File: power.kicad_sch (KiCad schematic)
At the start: 30 parts, among them U201 XC6206PxxxMR, U202 XR76208

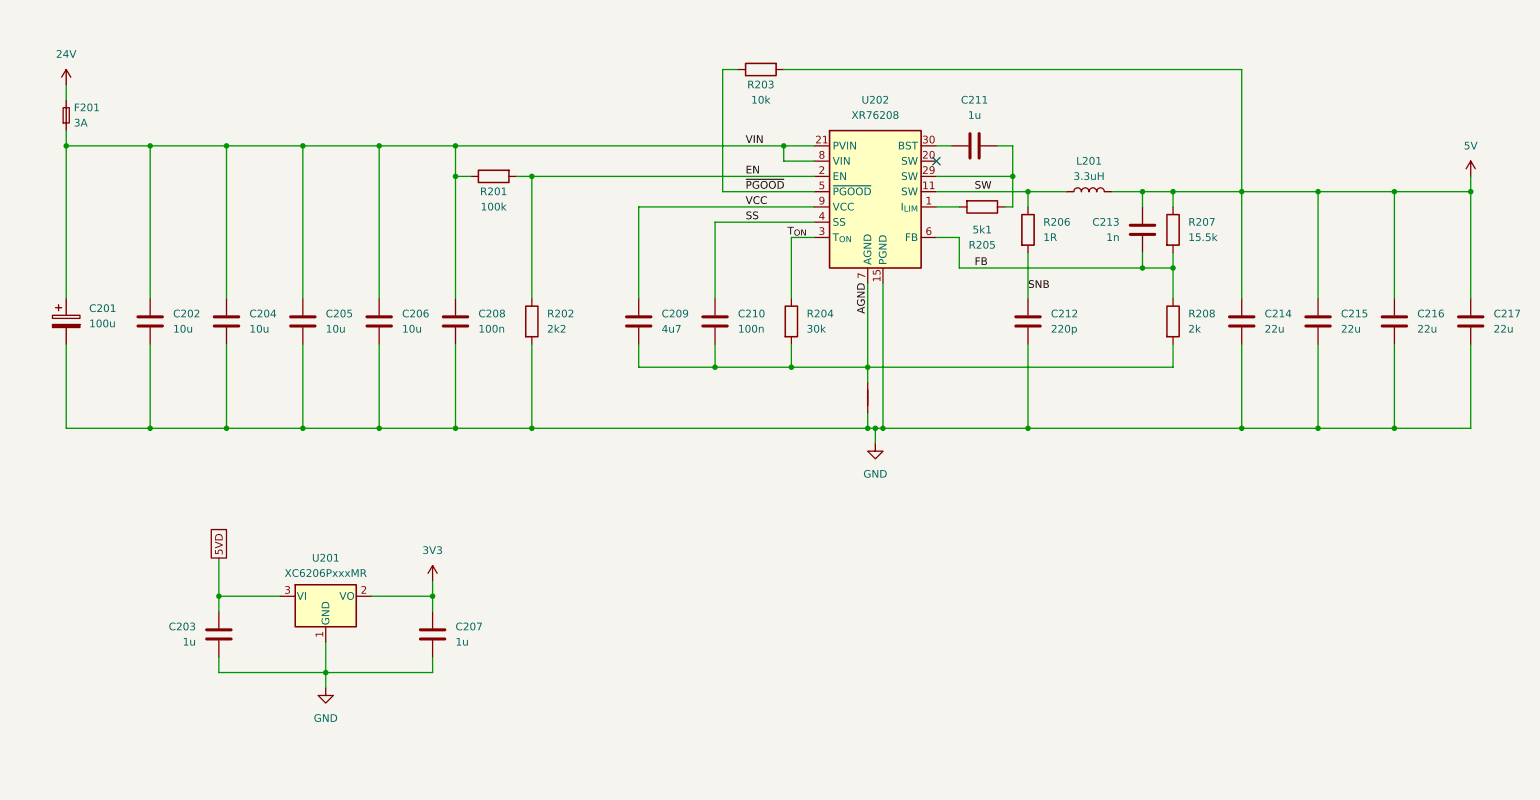
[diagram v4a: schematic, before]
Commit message: Rev 0.2: Major hardware improvements and production readiness
Hardware Improvements (Thanks to shx for schematic cleanup):
- Clean up schematic organization and structure
- Set CAN transceiver Silent pin to GND for stability
- Add status LEDs (yellow: 24V/5V/3.3V, green: MCU PB4)
- Replace jumpers with solder jumpers on bottom side
- Add jumpers to output PFETs for permanent-on without firmware
- Add robust test points for 5V/GND load testing
- Add optional heatsink for DC/DC converter on bottom
- Add 10µF capacitor for MCU on 3.3V rail

Component Optimizations:
- Replace 30kΩ with 33kΩ basic part for simplified BOM
- Change DC/DC feedback: 15.5kΩ15kΩ (new output: 5.1V)
- Upgrade CAN ESD protection: NUP2105LPESD1CAN
- Increase CAN termination resistor footprint: 04020603
- Switch USB hub supply from 5V to 3.3V per datasheet

Production Ready:
- Add all LCSC part numbers and rotations
- Generate complete production data package
- Improve PCB layout and button placement
- Create comprehensive changelog documentation
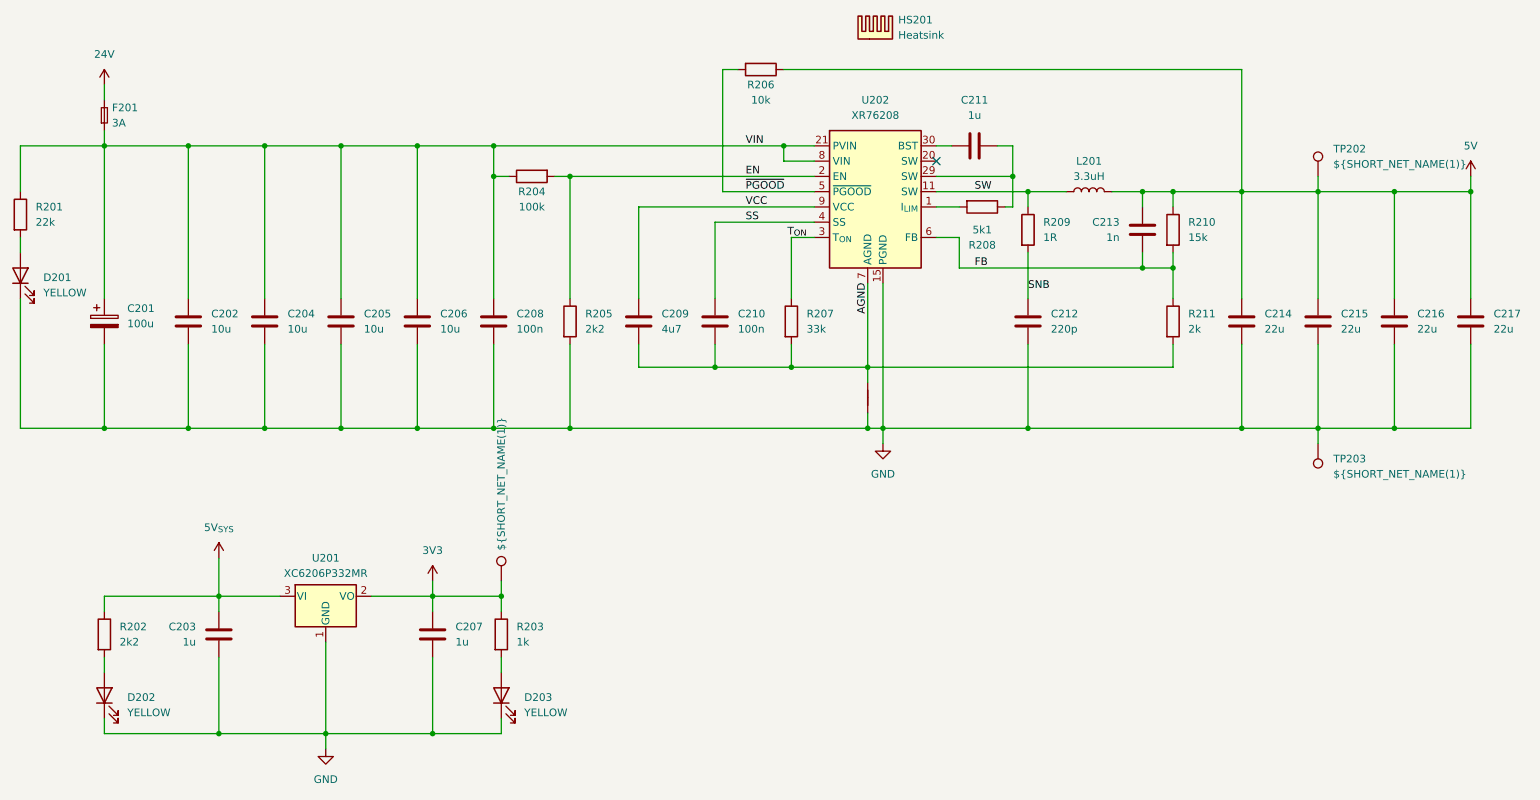
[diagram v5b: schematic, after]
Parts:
- added D201, D202, D203: YELLOW, LED_SMD:LED_0805_2012Metric, symbol Device:LED
- added HS201: Heatsink, project:HeatSink_9x9x5, symbol Mechanical:Heatsink
- added R201: 22k, Resistor_SMD:R_0402_1005Metric, symbol Device:R
- added R202: 2k2, Resistor_SMD:R_0402_1005Metric, symbol Device:R
- added R203: 1k, Resistor_SMD:R_0402_1005Metric, symbol Device:R
- added TP201: ${SHORT_NET_NAME(1)}, project:NAMED_TEST_POINT, symbol project:NamedTestPoint
- added TP202, TP203: ${SHORT_NET_NAME(1)}, TestPoint:TestPoint_Pad_D3.0mm, symbol Connector:TestPoint
- C203, C207, C211: LCSC Part # (none) -> C52923; Manufacturer Part # (none) -> CL05A105KA5NQNC
- C208, C210: LCSC Part # (none) -> C307331; Manufacturer Part # (none) -> CL05B104KB54PNC
- C212: LCSC Part # (none) -> C1603; Manufacturer Part # (none) -> CL10B221KB8NNNC
- C213: LCSC Part # (none) -> C1523; Manufacturer Part # (none) -> 0402B102K500NT
- C214, C215, C216, C217: LCSC Part # (none) -> C12891; Manufacturer Part # (none) -> CL31A226KAHNNNE
- F201: LCSC Part # (none) -> C163126; Manufacturer Part # (none) -> CFS12V3T3R00
- R204: renamed from R201; LCSC Part # (none) -> C25741; Manufacturer Part # (none) -> 0402WGF1003TCE
- R205: renamed from R202; LCSC Part # (none) -> C25879; Manufacturer Part # (none) -> 0402WGF2201TCE
- R206: renamed from R203; LCSC Part # (none) -> C25744; Manufacturer Part # (none) -> 0402WGF1002TCE
- R207: renamed from R204; value 30k -> 33k; LCSC Part # (none) -> C25779; Manufacturer Part # (none) -> 0402WGF3302TCE
- R208: renamed from R205; LCSC Part # (none) -> C25905; Manufacturer Part # (none) -> 0402WGF5101TCE
- R209: renamed from R206; LCSC Part # (none) -> C22936; Manufacturer Part # (none) -> 0603WAF100KT5E
- R210: renamed from R207; value 15.5k -> 15k; LCSC Part # (none) -> C25756; Manufacturer Part # (none) -> 0402WGF1502TCE
- R211: renamed from R208; LCSC Part # (none) -> C4109; Manufacturer Part # (none) -> 0402WGF2001TCE
- U201: value XC6206PxxxMR -> XC6206P332MR; LCSC Part # (none) -> C5446; Manufacturer Part # (none) -> XC6206P332MR-G
- U202: LCSC Part # (none) -> C555356; Manufacturer Part # (none) -> XR76208ELTR-F
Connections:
- net 3V3: now also R203.1, TP201.1
- net 5V: now also R206.1, TP202.1; no longer R206.2
- net AGND: no longer U202.31 (AGND)
- net GND: now also D201.1 (K), D202.1 (K), D203.1 (K), TP203.1
- net VIN: now also R201.1
- net ~{PGOOD}: now also R206.2; no longer R206.1
- net 5VD renamed 5V_{SYS}
- net 5V_{SYS}: now also R202.1
- new net: D202.2 (A), R202.2
- new net: D203.2 (A), R203.2
- new net: D201.2 (A), R201.2
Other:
- moved on the sheet: C201, C202, C204, C205, C206, C208, F201, R204, R205, R206

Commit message: Rev. 0.3: Add 10µF capacitor C304 to CAN transceiver and QR code placeholder
- Added 10µF capacitor C304 for improved CAN communication stability
- Added QR code placeholder for serial number on PCB
- Enhanced signal integrity with additional filtering at CAN transceiver
- Improved traceability with unique identification capability
- Updated changelogs and documentation for Rev. 0.3
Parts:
- U202: footprint project:IC_XR76203ELTR-F -> project:IC_XR76208ELTR-F
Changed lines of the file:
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@@
 			)
 		)
-		(property "Footprint" "project:IC_XR76203ELTR-F"
+		(property "Footprint" "project:IC_XR76208ELTR-F"
 			(at 163.83 63.5 0)
 			(effects

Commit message: Production Optimization: JLCPCB assembly improvements
- Excluded test points TP202/TP203 from BOM
- Set FT rotation offsets for automated assembly:
  - U202/U301: 270° rotation offset
  - U401: 180° rotation offset
- Updated production data for JLCPCB compatibility
- Added unreleased changelog section for tracking
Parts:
- TP202, TP203: now left out of the parts list
- U202: FT Rotation Offset (none) -> 270
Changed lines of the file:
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@@
 		(unit 1)
 		(exclude_from_sim no)
-		(in_bom yes)
+		(in_bom no)
 		(on_board yes)
 		(dnp no)
@@
 		(unit 1)
 		(exclude_from_sim no)
-		(in_bom yes)
+		(in_bom no)
 		(on_board yes)
 		(dnp no)
@@
 			(at 163.83 63.5 0)
 			(effects
+				(font
+					(size 1.27 1.27)
+				)
+				(hide yes)
+			)
+		)
+		(property "FT Rotation Offset" "270"
+			(at 163.83 63.5 0)
+			(effects

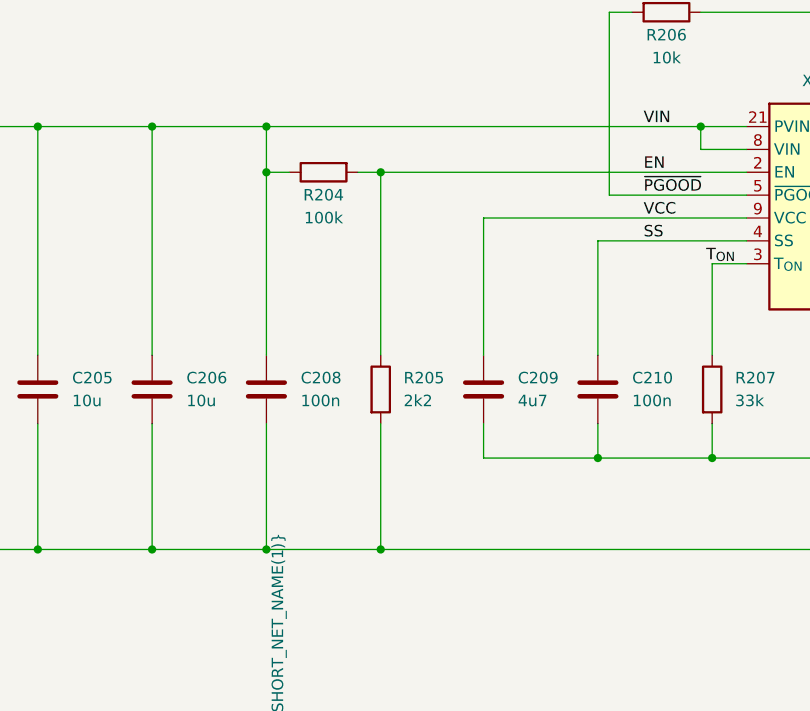
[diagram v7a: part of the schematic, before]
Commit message: docs: Update unreleased changes in changelog and README
- Fixed USB hub controller (U401/CH334): XO pin connected to GND for crystal-less operation
- Fixed DC/DC converter (U202/XR76208): Enable circuit changed to Zener diode for 12V operation
- Fixed USB outputs: Replaced fuses with TPS2557 power distribution switches for backfeed protection
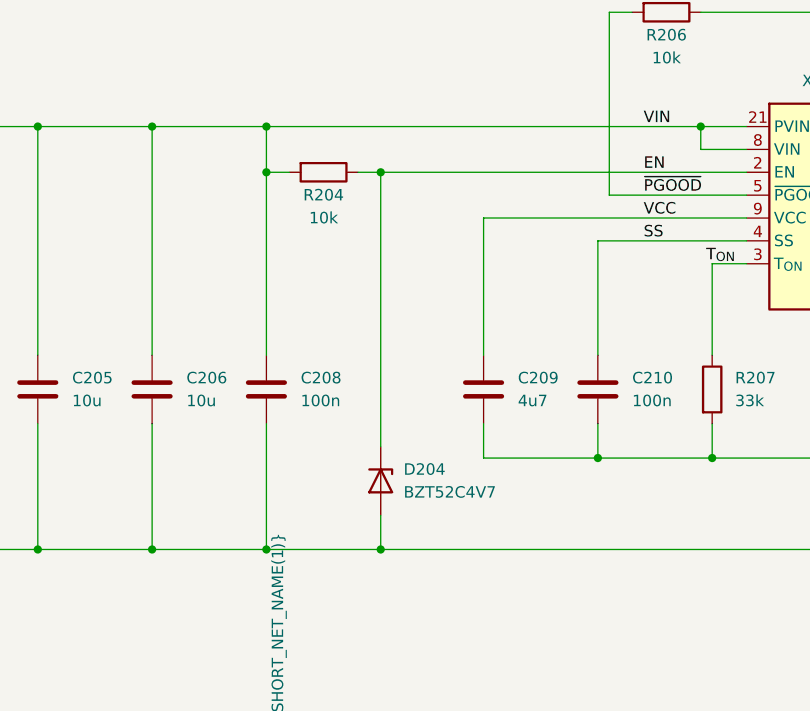
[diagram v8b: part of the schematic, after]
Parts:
- removed R205: 2k2, Resistor_SMD:R_0402_1005Metric, symbol Device:R
- added D204: BZT52C4V7, Diode_SMD:D_SOD-123, symbol Device:D_Zener
- R204: value 100k -> 10k; LCSC Part # C25741 -> C25744; Manufacturer Part # 0402WGF1003TCE -> 0402WGF1002TCE
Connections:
- net EN: now also R204.1, D204.1 (K); no longer R204.2
- net GND: now also D204.2 (A)
- net VIN: now also R204.2; no longer R204.1
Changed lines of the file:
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@@
 	(generator "eeschema")
 	(generator_version "9.0")
-	(paper "A4")
+	(paper "A3")
 	(title_block
 		(title "EWS - Power, CANbus and USB HAT for 3D Printers")
@@
 	(wire
 		(pts
-			(xy 113.03 87.63) (xy 113.03 101.6)
+			(xy 113.03 97.79) (xy 113.03 101.6)
 		)
 		(stroke
@@
 	(wire
 		(pts
-			(xy 113.03 59.69) (xy 113.03 80.01)
+			(xy 113.03 59.69) (xy 113.03 90.17)
 		)
 		(stroke
@@
 	)
 	(symbol
-		(lib_id "Device:R")
-		(at 113.03 83.82 0)
-		(unit 1)
-		(exclude_from_sim no)
-		(in_bom yes)
-		(on_board yes)
-		(dnp no)
-		(fields_autoplaced yes)
-		(property "Reference" "R205"
-			(at 115.57 82.5499 0)
-			(effects
-				(font
-					(size 1.27 1.27)
-				)
-				(justify left)
-			)
-		)
-		(property "Value" "2k2"
-			(at 115.57 85.0899 0)
-			(effects
-				(font
-					(size 1.27 1.27)
-				)
-				(justify left)
-			)
-		)
-		(property "Footprint" "Resistor_SMD:R_0402_1005Metric"
-			(at 111.252 83.82 90)
-			(effects
-				(font
-					(size 1.27 1.27)
-				)
-				(hide yes)
-			)
-		)
-		(property "Datasheet" "~"
-			(at 113.03 83.82 0)
-			(effects
-				(font
-					(size 1.27 1.27)
-				)
-				(hide yes)
-			)
-		)
-		(property "Description" "Resistor"
-			(at 113.03 83.82 0)
-			(effects
-				(font
-					(size 1.27 1.27)
-				)
-				(hide yes)
-			)
-		)
-		(property "LCSC Part #" "C25879"
-			(at 113.03 83.82 0)
-			(effects
-				(font
-					(size 1.27 1.27)
-				)
-				(hide yes)
-			)
-		)
-		(property "Manufacturer Part #" "0402WGF2201TCE"
-			(at 113.03 83.82 0)
-			(effects
-				(font
-					(size 1.27 1.27)
-				)
-				(hide yes)
-			)
-		)
-		(pin "1"
-		)
-		(pin "2"
-		)
-		(instances
-			(project "EWS"
-				(path "/4ae99543-64c8-472f-befd-04c32f138656/e94b5c4c-885f-4cd2-8976-23421227f36b"
-					(reference "R205")
-					(unit 1)
-				)
-			)
-		)
-	)
-	(symbol
 		(lib_id "Device:C")
 		(at 62.23 83.82 0)
@@
 	)
 	(symbol
+		(lib_id "Device:D_Zener")
+		(at 113.03 93.98 270)
+		(unit 1)
+		(exclude_from_sim no)
+		(in_bom yes)
+		(on_board yes)
+		(dnp no)
+		(fields_autoplaced yes)
+		(property "Reference" "D204"
+			(at 115.57 92.7099 90)
+			(effects
+				(font
+					(size 1.27 1.27)
+				)
+				(justify left)
+			)
+		)
+		(property "Value" "BZT52C4V7"
+			(at 115.57 95.2499 90)
+			(effects
+				(font
+					(size 1.27 1.27)
+				)
+				(justify left)
+			)
+		)
+		(property "Footprint" "Diode_SMD:D_SOD-123"
+			(at 113.03 93.98 0)
+			(effects
+				(font
+					(size 1.27 1.27)
+				)
+				(hide yes)
+			)
+		)
+		(property "Datasheet" "~"
+			(at 113.03 93.98 0)
+			(effects
+				(font
+					(size 1.27 1.27)
+				)
+				(hide yes)
+			)
+		)
+		(property "Description" "Zener diode"
+			(at 113.03 93.98 0)
+			(effects
+				(font
+					(size 1.27 1.27)
+				)
+				(hide yes)
+			)
+		)
+		(property "Manufacturer Part #" "BZT52C4V7"
+			(at 113.03 93.98 0)
+			(effects
+				(font
+					(size 1.27 1.27)
+				)
+				(hide yes)
+			)
+		)
+		(property "LCSC Part #" "C19077400"
+			(at 113.03 93.98 0)
+			(effects
+				(font
+					(size 1.27 1.27)
+				)
+				(hide yes)
+			)
+		)
+		(property "FT Rotation Offset" ""
+			(at 113.03 93.98 0)
+			(effects
+				(font
+					(size 1.27 1.27)
+				)
+				(hide yes)
+			)
+		)
+		(pin "2"
+		)
+		(pin "1"
+		)
+		(instances
+			(project ""
+				(path "/4ae99543-64c8-472f-befd-04c32f138656/e94b5c4c-885f-4cd2-8976-23421227f36b"
+					(reference "D204")
+					(unit 1)
+				)
+			)
+		)
+	)
+	(symbol
 		(lib_id "Device:R")
 		(at 21.59 66.04 0)
@@
 	)
 	(symbol
-		(lib_id "Device:R")
-		(at 106.68 59.69 90)
-		(mirror x)
-		(unit 1)
-		(exclude_from_sim no)
-		(in_bom yes)
-		(on_board yes)
-		(dnp no)
-		(property "Reference" "R204"
-			(at 106.68 62.23 90)
-			(effects
-				(font
-					(size 1.27 1.27)
-				)
-			)
-		)
-		(property "Value" "100k"
-			(at 106.68 64.77 90)
-			(effects
-				(font
-					(size 1.27 1.27)
-				)
-			)
-		)
-		(property "Footprint" "Resistor_SMD:R_0402_1005Metric"
-			(at 106.68 57.912 90)
-			(effects
-				(font
-					(size 1.27 1.27)
-				)
-				(hide yes)
-			)
-		)
-		(property "Datasheet" "~"
-			(at 106.68 59.69 0)
-			(effects
-				(font
-					(size 1.27 1.27)
-				)
-				(hide yes)
-			)
-		)
-		(property "Description" "Resistor"
-			(at 106.68 59.69 0)
-			(effects
-				(font
-					(size 1.27 1.27)
-				)
-				(hide yes)
-			)
-		)
-		(property "Manufacturer Part #" "0402WGF1003TCE"
-			(at 106.68 59.69 0)
-			(effects
-				(font
-					(size 1.27 1.27)
-				)
-				(hide yes)
-			)
-		)
-		(property "LCSC Part #" "C25741"
-			(at 106.68 59.69 0)
-			(effects
-				(font
-					(size 1.27 1.27)
-				)
-				(hide yes)
-			)
-		)
-		(property "FT Rotation Offset" ""
-			(at 106.68 59.69 0)
-			(effects
-				(font
-					(size 1.27 1.27)
-				)
-				(hide yes)
-			)
-		)
-		(pin "1"
-		)
-		(pin "2"
-		)
-		(instances
-			(project ""
-				(path "/4ae99543-64c8-472f-befd-04c32f138656/e94b5c4c-885f-4cd2-8976-23421227f36b"
-					(reference "R204")
-					(unit 1)
-				)
-			)
-		)
-	)
-	(symbol
 		(lib_id "Device:C")
 		(at 262.89 83.82 0)
@@
 					(unit 1)
 				)
+			)
+		)
+	)
+	(symbol
+		(lib_id "Device:R")
+		(at 106.68 59.69 270)
+		(unit 1)
+		(exclude_from_sim no)
+		(in_bom yes)
+		(on_board yes)
+		(dnp no)
+		(property "Reference" "R204"
+			(at 106.68 62.23 90)
+			(effects
+				(font
+					(size 1.27 1.27)
+				)
+			)
+		)
+		(property "Value" "10k"
+			(at 106.68 64.77 90)
+			(effects
+				(font
+					(size 1.27 1.27)
+				)
+			)
+		)
+		(property "Footprint" "Resistor_SMD:R_0402_1005Metric"
+			(at 106.68 57.912 90)
+			(effects
+				(font
+					(size 1.27 1.27)
+				)
+				(hide yes)
+			)
+		)
+		(property "Datasheet" "~"
+			(at 106.68 59.69 0)
+			(effects
+				(font
+					(size 1.27 1.27)
+				)
+				(hide yes)
+			)
+		)
+		(property "Description" "Resistor"
+			(at 106.68 59.69 0)
+			(effects
+				(font
+					(size 1.27 1.27)
+				)
+				(hide yes)
+			)
+		)
+		(property "LCSC Part #" "C25744"
+			(at 106.68 59.69 90)
+			(effects
+				(font
+					(size 1.27 1.27)
+				)
+				(hide yes)
+			)
+		)
+		(property "Manufacturer Part #" "0402WGF1002TCE"
+			(at 106.68 59.69 90)
+			(effects
+				(font
+					(size 1.27 1.27)
+				)
+				(hide yes)
+			)
+		)
+		(pin "1"
+		)
+		(pin "2"
+		)
+		(instances
+			(project "EWS"
+				(path "/4ae99543-64c8-472f-befd-04c32f138656/e94b5c4c-885f-4cd2-8976-23421227f36b"
+					(reference "R204")
+					(unit 1)
+				)
